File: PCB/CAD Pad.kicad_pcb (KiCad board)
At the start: 2 copper layers, 68.5 x 100 mm, 34 parts, among them J1 Conn_01x04, SW1 SW_Push, SW10 SW_Push, SW11 SW_Push, SW12 SW_Push, SW13 RotaryEncoder_Switch, SW2 SW_Push, SW3 SW_Push, SW4 SW_Push, SW5 SW_Push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

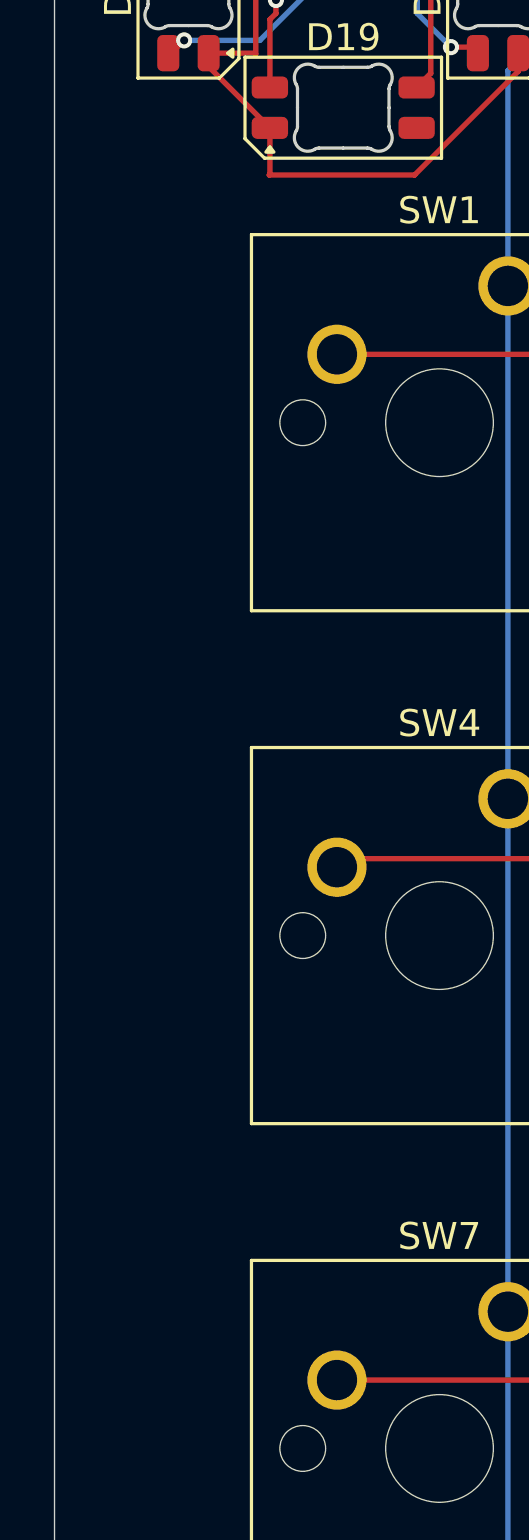
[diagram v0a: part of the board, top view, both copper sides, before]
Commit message: Add Git username to parts
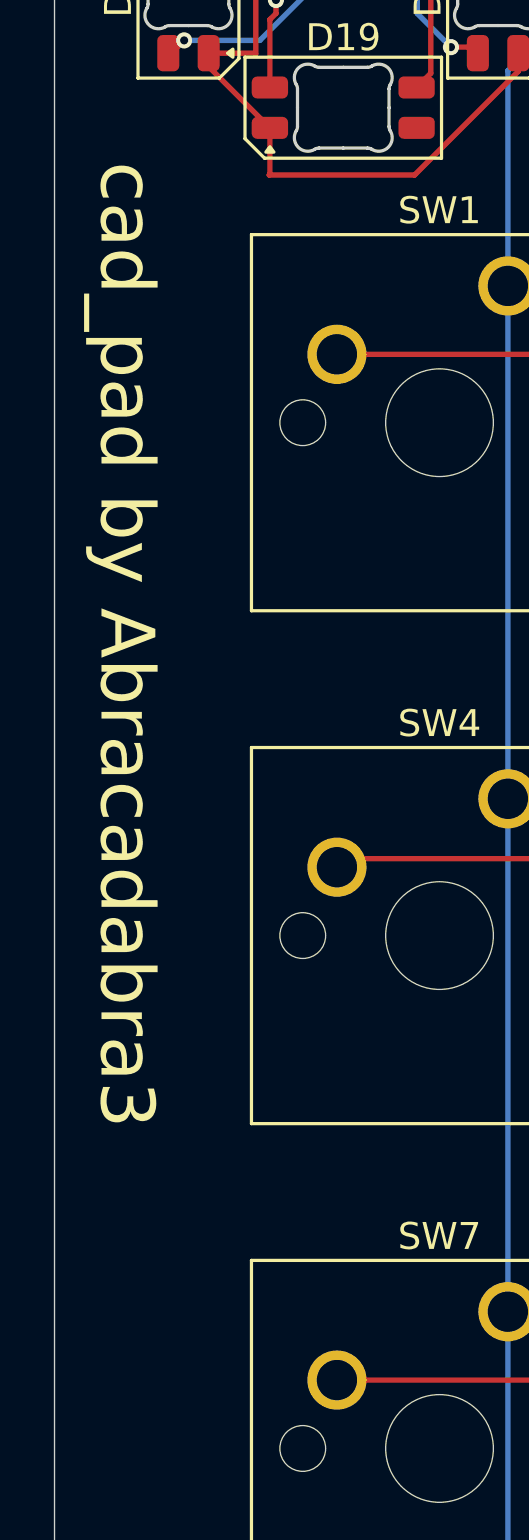
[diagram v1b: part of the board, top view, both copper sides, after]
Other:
- board text added: "cad_pad by Abracadabra3"
